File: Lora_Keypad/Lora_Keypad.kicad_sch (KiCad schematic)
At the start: 2 parts, among them U1 Heltec_Wifi_LoRa_V1

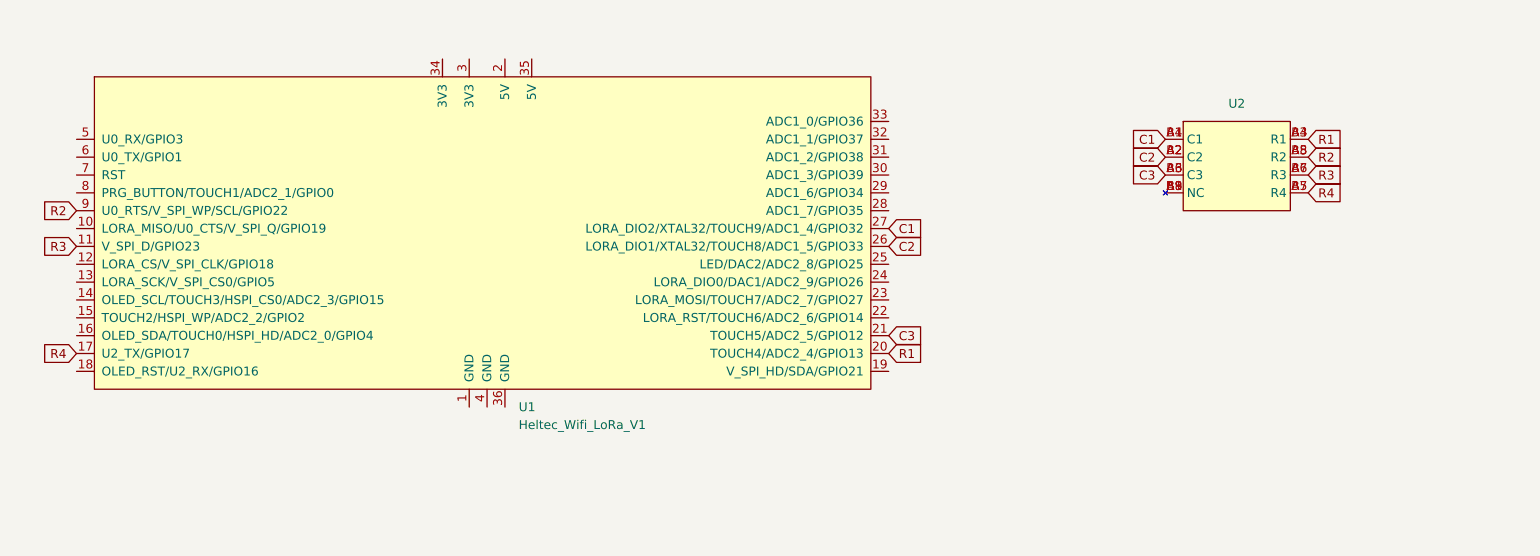
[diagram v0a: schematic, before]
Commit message: added debug header
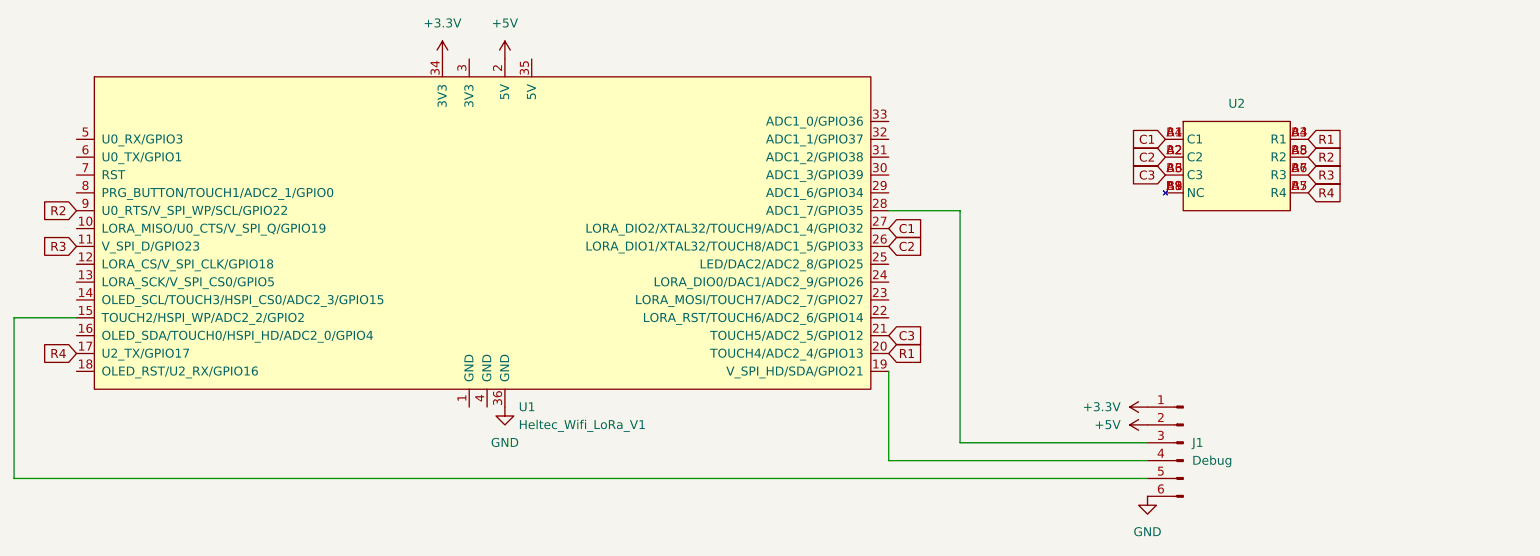
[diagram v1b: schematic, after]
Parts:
- added J1: Debug, Connector_PinHeader_2.54mm:PinHeader_1x06_P2.54mm_Vertical, symbol Connector:Conn_01x06_Pin
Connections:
- net at U1.15 (TOUCH2/HSPI_WP/ADC2_2/GPIO2): now also J1.5 (Pin_5)
- net at U1.19 (V_SPI_HD/SDA/GPIO21): now also J1.4 (Pin_4)
- net +5V: now reaches U1.2 (5V)
- net +5V: now also J1.2 (Pin_2)
- net at U1.28 (ADC1_7/GPIO35): now also J1.3 (Pin_3)
- net +3.3V: now reaches U1.34 (3V3)
- net +3.3V: now also J1.1 (Pin_1)
- net GND: now reaches U1.36 (GND)
- net GND: now also J1.6 (Pin_6)
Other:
- title: (none) -> Lora Keypad
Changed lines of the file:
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@@
 (kicad_sch (version 20230121) (generator eeschema)
   (paper "A4")
+  (title_block
+    (title "Lora Keypad")
+    (date "2023-08-30")
+    (rev "v1")
+  )
+  (wire (pts (xy 165.1 110.49) (xy 175.26 110.49))
+    (stroke (width 0) (type default))
+  )
+  (wire (pts (xy 40.64 148.59) (xy 201.93 148.59))
+    (stroke (width 0) (type default))
+  )
+  (wire (pts (xy 165.1 146.05) (xy 165.1 133.35))
+    (stroke (width 0) (type default))
+  )
+  (wire (pts (xy 175.26 143.51) (xy 201.93 143.51))
+    (stroke (width 0) (type default))
+  )
+  (wire (pts (xy 201.93 146.05) (xy 165.1 146.05))
+    (stroke (width 0) (type default))
+  )
+  (wire (pts (xy 49.53 125.73) (xy 40.64 125.73))
+    (stroke (width 0) (type default))
+  )
+  (wire (pts (xy 175.26 110.49) (xy 175.26 143.51))
+    (stroke (width 0) (type default))
+  )
+  (wire (pts (xy 40.64 125.73) (xy 40.64 148.59))
+    (stroke (width 0) (type default))
+  )
   (global_label "R3" (shape input) (at 49.53 115.57 180) (fields_autoplaced)
     (effects (font (size 1.27 1.27)) (justify right))
@@
     (property "Intersheetrefs" "${INTERSHEET_REFS}" (at 230.1753 102.87 0)
       (effects (font (size 1.27 1.27)) (justify left) hide)
+    )
+  )
+  (symbol (lib_id "power:+3.3V") (at 101.6 88.9 0) (unit 1)
+    (in_bom yes) (on_board yes) (dnp no) (fields_autoplaced)
+    (property "Reference" "#PWR04" (at 101.6 92.71 0)
+      (effects (font (size 1.27 1.27)) hide)
+    )
+    (property "Value" "+3.3V" (at 101.6 83.82 0)
+      (effects (font (size 1.27 1.27)))
+    )
+    (property "Footprint" "" (at 101.6 88.9 0)
+      (effects (font (size 1.27 1.27)) hide)
+    )
+    (property "Datasheet" "" (at 101.6 88.9 0)
+      (effects (font (size 1.27 1.27)) hide)
+    )
+    (pin "1")
+    (instances
+      (project "Lora_Keypad"
+        (path "/c8d40c8d-f0b0-48e3-af03-02b40e7fa894"
+          (reference "#PWR04") (unit 1)
+        )
+      )
+    )
+  )
+  (symbol (lib_id "power:GND") (at 201.93 151.13 0) (unit 1)
+    (in_bom yes) (on_board yes) (dnp no) (fields_autoplaced)
+    (property "Reference" "#PWR02" (at 201.93 157.48 0)
+      (effects (font (size 1.27 1.27)) hide)
+    )
+    (property "Value" "GND" (at 201.93 156.21 0)
+      (effects (font (size 1.27 1.27)))
+    )
+    (property "Footprint" "" (at 201.93 151.13 0)
+      (effects (font (size 1.27 1.27)) hide)
+    )
+    (property "Datasheet" "" (at 201.93 151.13 0)
+      (effects (font (size 1.27 1.27)) hide)
+    )
+    (pin "1")
+    (instances
+      (project "Lora_Keypad"
+        (path "/c8d40c8d-f0b0-48e3-af03-02b40e7fa894"
+          (reference "#PWR02") (unit 1)
+        )
+      )
     )
   )
@@
         )
       )
+    )
+  )
+  (symbol (lib_id "power:+5V") (at 110.49 88.9 0) (unit 1)
+    (in_bom yes) (on_board yes) (dnp no) (fields_autoplaced)
+    (property "Reference" "#PWR03" (at 110.49 92.71 0)
+      (effects (font (size 1.27 1.27)) hide)
+    )
+    (property "Value" "+5V" (at 110.49 83.82 0)
+      (effects (font (size 1.27 1.27)))
+    )
+    (property "Footprint" "" (at 110.49 88.9 0)
+      (effects (font (size 1.27 1.27)) hide)
+    )
+    (property "Datasheet" "" (at 110.49 88.9 0)
+      (effects (font (size 1.27 1.27)) hide)
+    )
+    (pin "1")
+    (instances
+      (project "Lora_Keypad"
+        (path "/c8d40c8d-f0b0-48e3-af03-02b40e7fa894"
+          (reference "#PWR03") (unit 1)
+        )
+      )
+    )
+  )
+  (symbol (lib_id "power:GND") (at 110.49 138.43 0) (unit 1)
+    (in_bom yes) (on_board yes) (dnp no) (fields_autoplaced)
+    (property "Reference" "#PWR01" (at 110.49 144.78 0)
+      (effects (font (size 1.27 1.27)) hide)
+    )
+    (property "Value" "GND" (at 110.49 143.51 0)
+      (effects (font (size 1.27 1.27)))
+    )
+    (property "Footprint" "" (at 110.49 138.43 0)
+      (effects (font (size 1.27 1.27)) hide)
+    )
+    (property "Datasheet" "" (at 110.49 138.43 0)
+      (effects (font (size 1.27 1.27)) hide)
+    )
+    (pin "1")
+    (instances
+      (project "Lora_Keypad"
+        (path "/c8d40c8d-f0b0-48e3-af03-02b40e7fa894"
+          (reference "#PWR01") (unit 1)
+        )
+      )
+    )
+  )
+  (symbol (lib_id "power:+3.3V") (at 201.93 138.43 90) (unit 1)
+    (in_bom yes) (on_board yes) (dnp no) (fields_autoplaced)
+    (property "Reference" "#PWR05" (at 205.74 138.43 0)
+      (effects (font (size 1.27 1.27)) hide)
+    )
+    (property "Value" "+3.3V" (at 198.12 138.43 90)
+      (effects (font (size 1.27 1.27)) (justify left))
+    )
+    (property "Footprint" "" (at 201.93 138.43 0)
+      (effects (font (size 1.27 1.27)) hide)
+    )
+    (property "Datasheet" "" (at 201.93 138.43 0)
+      (effects (font (size 1.27 1.27)) hide)
+    )
+    (pin "1")
+    (instances
+      (project "Lora_Keypad"
+        (path "/c8d40c8d-f0b0-48e3-af03-02b40e7fa894"
+          (reference "#PWR05") (unit 1)
+        )
+      )
+    )
+  )
+  (symbol (lib_id "Connector:Conn_01x06_Pin") (at 207.01 143.51 0) (mirror y) (unit 1)
+    (in_bom yes) (on_board yes) (dnp no) (fields_autoplaced)
+    (property "Reference" "J1" (at 208.28 143.51 0)
+      (effects (font (size 1.27 1.27)) (justify right))
+    )
+    (property "Value" "Debug" (at 208.28 146.05 0)
+      (effects (font (size 1.27 1.27)) (justify right))
+    )
+    (property "Footprint" "Connector_PinHeader_2.54mm:PinHeader_1x06_P2.54mm_Vertical" (at 207.01 143.51 0)
+      (effects (font (size 1.27 1.27)) hide)
+    )
+    (property "Datasheet" "~" (at 207.01 143.51 0)
+      (effects (font (size 1.27 1.27)) hide)
+    )
+    (pin "1")
+    (pin "2")
+    (pin "3")
+    (pin "4")
+    (pin "5")
+    (pin "6")
+    (instances
+      (project "Lora_Keypad"
+        (path "/c8d40c8d-f0b0-48e3-af03-02b40e7fa894"
+          (reference "J1") (unit 1)
+        )
+      )
+    )
+  )
+  (symbol (lib_id "power:+5V") (at 201.93 140.97 90) (unit 1)
+    (in_bom yes) (on_board yes) (dnp no) (fields_autoplaced)
+    (property "Reference" "#PWR06" (at 205.74 140.97 0)
+      (effects (font (size 1.27 1.27)) hide)
+    )
+    (property "Value" "+5V" (at 198.12 140.97 90)
+      (effects (font (size 1.27 1.27)) (justify left))
+    )
+    (property "Footprint" "" (at 201.93 140.97 0)
+      (effects (font (size 1.27 1.27)) hide)
+    )
+    (property "Datasheet" "" (at 201.93 140.97 0)
+      (effects (font (size 1.27 1.27)) hide)
+    )
+    (pin "1")
+    (instances
+      (project "Lora_Keypad"
+        (path "/c8d40c8d-f0b0-48e3-af03-02b40e7fa894"
+          (reference "#PWR06") (unit 1)
+        )
+      )

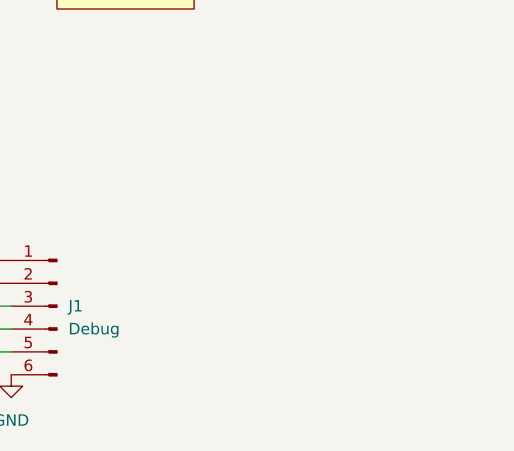
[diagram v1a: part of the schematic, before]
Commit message: added mounting wholes
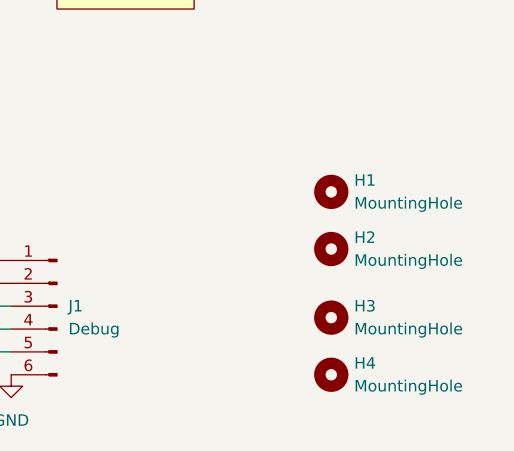
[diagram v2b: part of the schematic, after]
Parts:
- added H1, H2, H3, H4: MountingHole, MountingHole:MountingHole_3.2mm_M3, symbol Mechanical:MountingHole
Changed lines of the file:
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@@
+    )
+  )
+  (symbol (lib_id "Mechanical:MountingHole") (at 237.49 130.81 0) (unit 1)
+    (in_bom yes) (on_board yes) (dnp no) (fields_autoplaced)
+    (property "Reference" "H1" (at 240.03 129.54 0)
+      (effects (font (size 1.27 1.27)) (justify left))
+    )
+    (property "Value" "MountingHole" (at 240.03 132.08 0)
+      (effects (font (size 1.27 1.27)) (justify left))
+    )
+    (property "Footprint" "MountingHole:MountingHole_3.2mm_M3" (at 237.49 130.81 0)
+      (effects (font (size 1.27 1.27)) hide)
+    )
+    (property "Datasheet" "~" (at 237.49 130.81 0)
+      (effects (font (size 1.27 1.27)) hide)
+    )
+    (instances
+      (project "Lora_Keypad"
+        (path "/c8d40c8d-f0b0-48e3-af03-02b40e7fa894"
+          (reference "H1") (unit 1)
+        )
+      )
     )
   )
@@
         (path "/c8d40c8d-f0b0-48e3-af03-02b40e7fa894"
           (reference "U2") (unit 1)
+        )
+      )
+    )
+  )
+  (symbol (lib_id "Mechanical:MountingHole") (at 237.49 151.13 0) (unit 1)
+    (in_bom yes) (on_board yes) (dnp no) (fields_autoplaced)
+    (property "Reference" "H4" (at 240.03 149.86 0)
+      (effects (font (size 1.27 1.27)) (justify left))
+    )
+    (property "Value" "MountingHole" (at 240.03 152.4 0)
+      (effects (font (size 1.27 1.27)) (justify left))
+    )
+    (property "Footprint" "MountingHole:MountingHole_3.2mm_M3" (at 237.49 151.13 0)
+      (effects (font (size 1.27 1.27)) hide)
+    )
+    (property "Datasheet" "~" (at 237.49 151.13 0)
+      (effects (font (size 1.27 1.27)) hide)
+    )
+    (instances
+      (project "Lora_Keypad"
+        (path "/c8d40c8d-f0b0-48e3-af03-02b40e7fa894"
+          (reference "H4") (unit 1)
         )
       )
@@
         )
       )
+    )
+  )
+  (symbol (lib_id "Mechanical:MountingHole") (at 237.49 144.78 0) (unit 1)
+    (in_bom yes) (on_board yes) (dnp no) (fields_autoplaced)
+    (property "Reference" "H3" (at 240.03 143.51 0)
+      (effects (font (size 1.27 1.27)) (justify left))
+    )
+    (property "Value" "MountingHole" (at 240.03 146.05 0)
+      (effects (font (size 1.27 1.27)) (justify left))
+    )
+    (property "Footprint" "MountingHole:MountingHole_3.2mm_M3" (at 237.49 144.78 0)
+      (effects (font (size 1.27 1.27)) hide)
+    )
+    (property "Datasheet" "~" (at 237.49 144.78 0)
+      (effects (font (size 1.27 1.27)) hide)
+    )
+    (instances
+      (project "Lora_Keypad"
+        (path "/c8d40c8d-f0b0-48e3-af03-02b40e7fa894"
+          (reference "H3") (unit 1)
+        )
+      )
+    )
+  )
+  (symbol (lib_id "Mechanical:MountingHole") (at 237.49 137.16 0) (unit 1)
+    (in_bom yes) (on_board yes) (dnp no) (fields_autoplaced)
+    (property "Reference" "H2" (at 240.03 135.89 0)
+      (effects (font (size 1.27 1.27)) (justify left))
+    )
+    (property "Value" "MountingHole" (at 240.03 138.43 0)
+      (effects (font (size 1.27 1.27)) (justify left))
+    )
+    (property "Footprint" "MountingHole:MountingHole_3.2mm_M3" (at 237.49 137.16 0)
+      (effects (font (size 1.27 1.27)) hide)
+    )
+    (property "Datasheet" "~" (at 237.49 137.16 0)
+      (effects (font (size 1.27 1.27)) hide)
+    )
+    (instances
+      (project "Lora_Keypad"
+        (path "/c8d40c8d-f0b0-48e3-af03-02b40e7fa894"
+          (reference "H2") (unit 1)
+        )
+      )
